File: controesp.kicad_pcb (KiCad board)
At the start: 2 copper layers, 216.9 x 86.5 mm, 71 parts, among them J1 Screw_Terminal_01x08, J13 Conn_01x19_Socket, J14 Conn_01x16_Socket, J15 Screw_Terminal_01x02, J16 Conn_01x19_Socket, J17 Conn_01x19_Socket, J2 Screw_Terminal_01x04, J3 Conn_01x14_Socket, J4 Conn_01x14_Pin, J5 Conn_01x16_Pin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

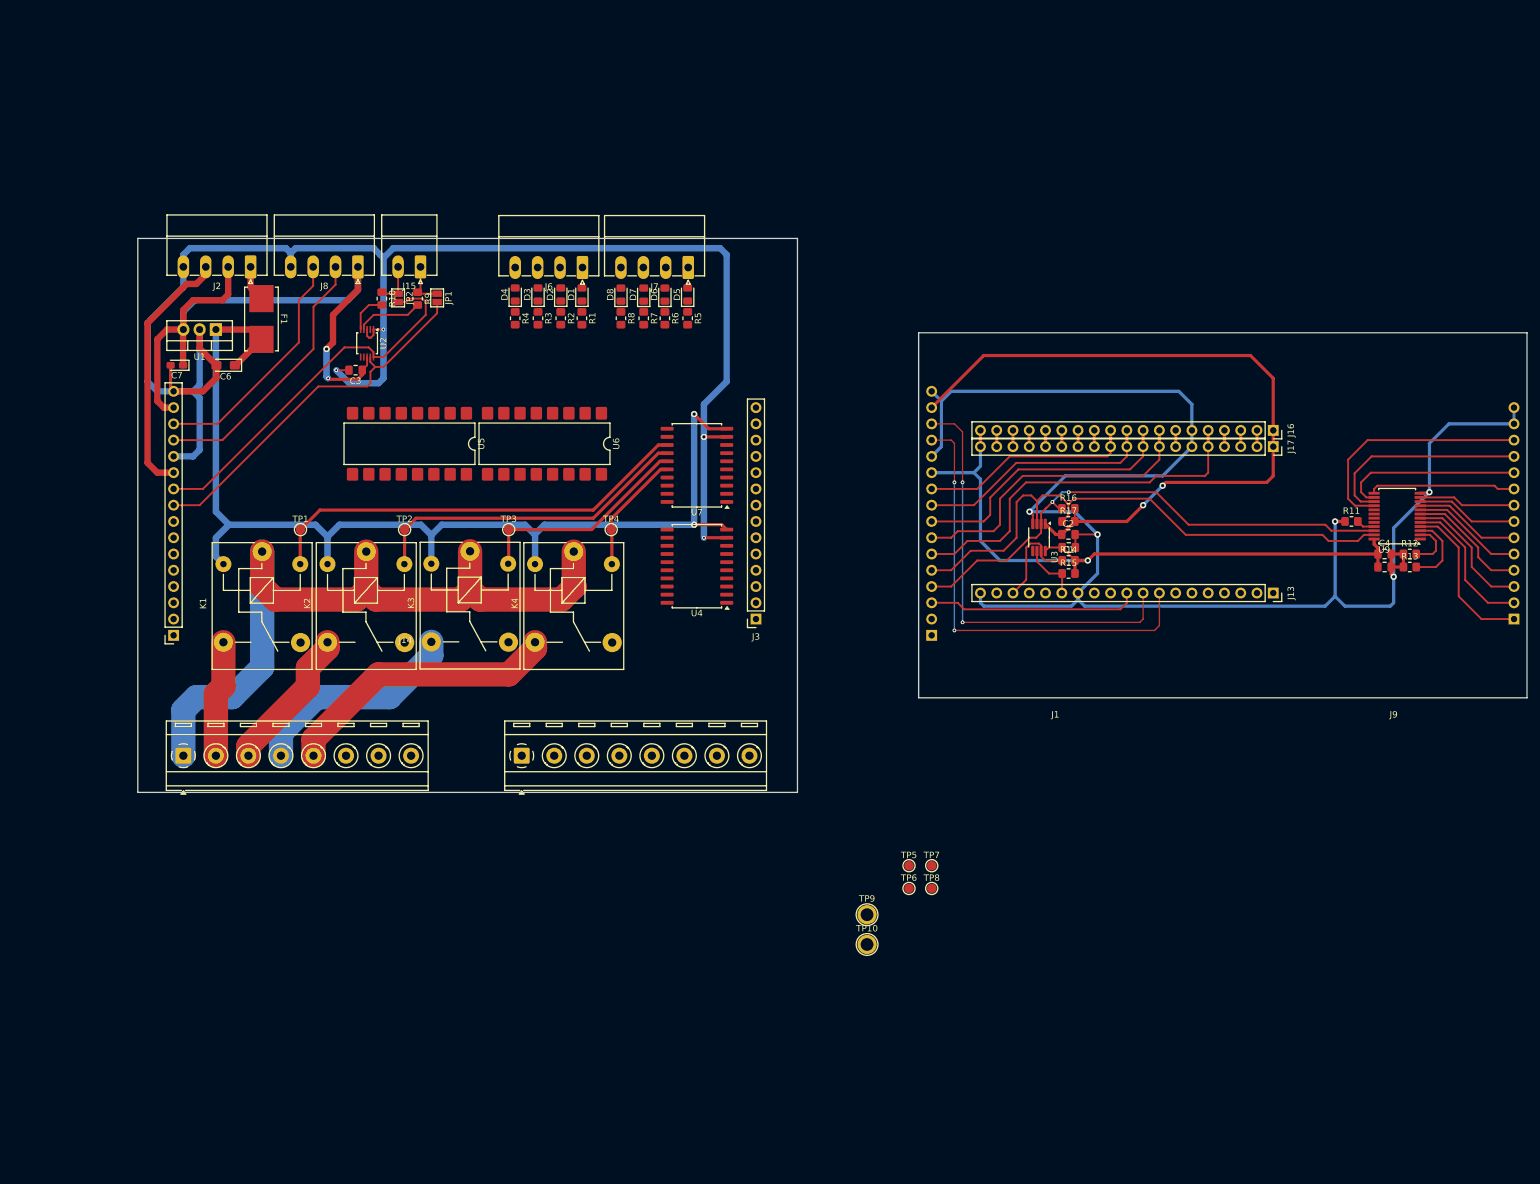
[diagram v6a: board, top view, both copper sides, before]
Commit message: pcb layout finished
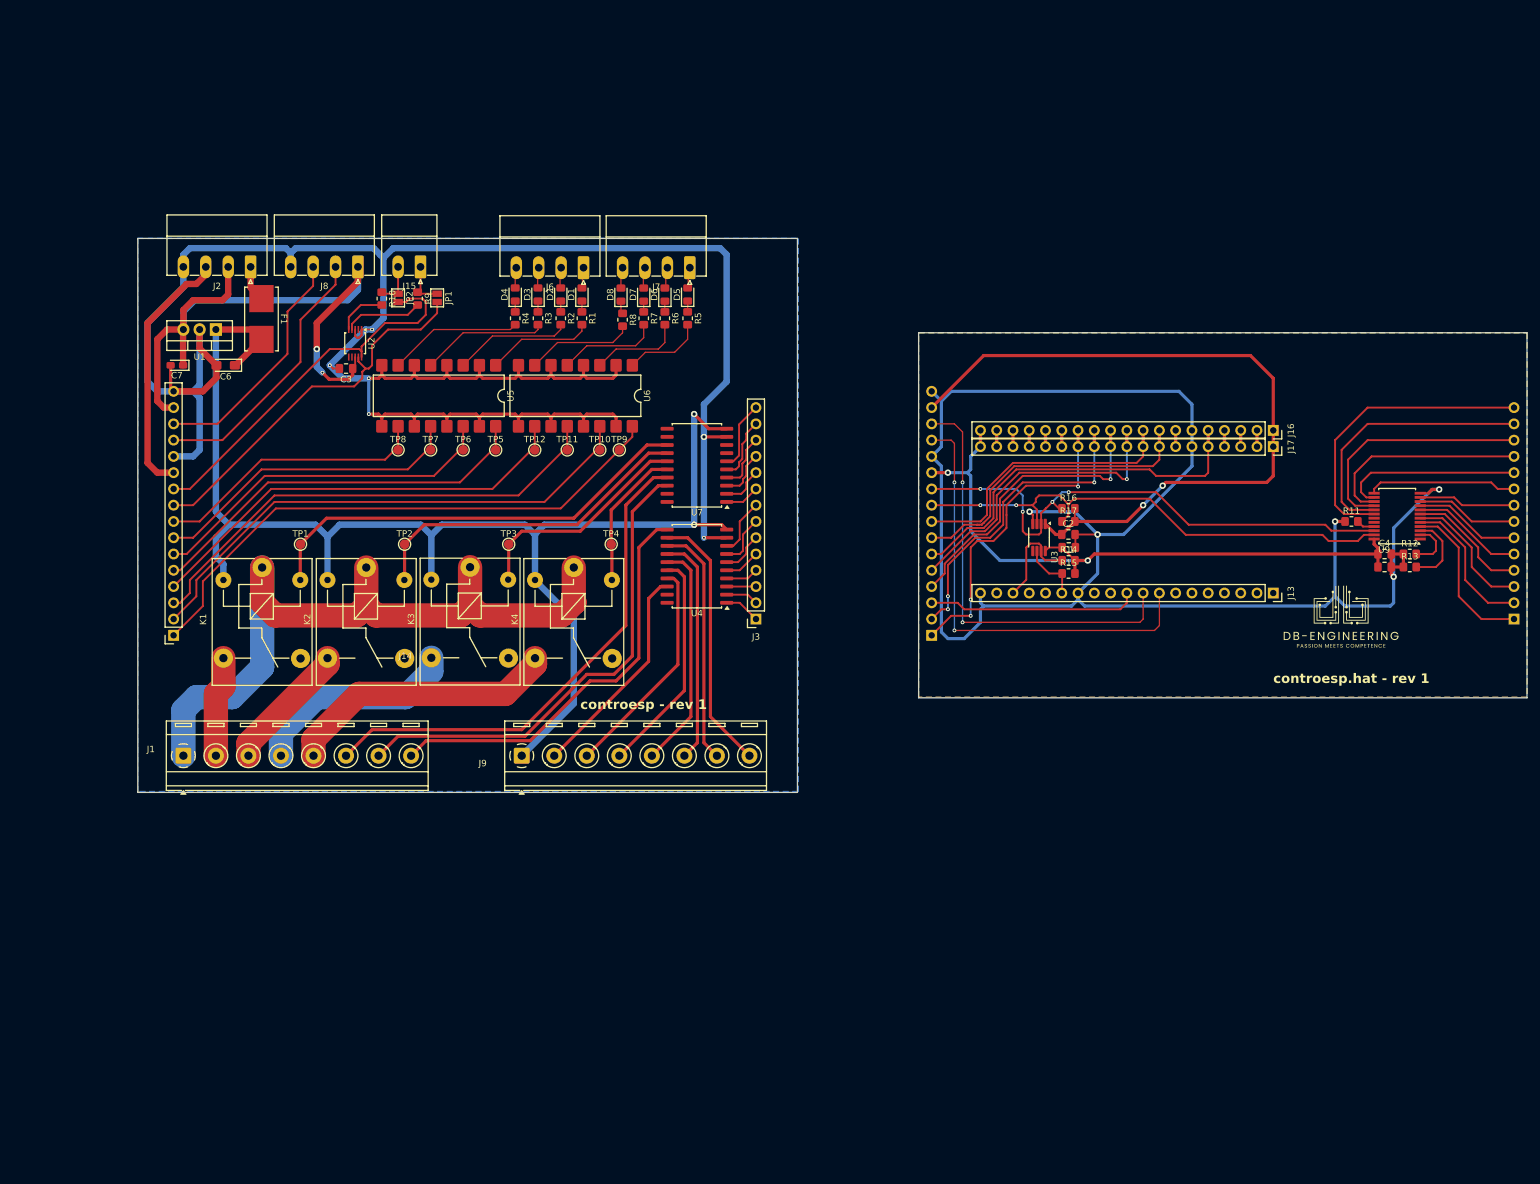
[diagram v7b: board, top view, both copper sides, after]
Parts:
- added G***: LOGO, graphics:db_engineering_logo, F.Cu at (237.7, 109.2)
- added G***: LOGO, graphics:db_engineering_logo, B.Cu at (73.2, 81.3)
- added TP11: ~, TestPoint:TestPoint_Pad_D1.5mm, F.Cu at (116.8, 82.8)
- added TP12: ~, TestPoint:TestPoint_Pad_D1.5mm, F.Cu at (111.8, 82.8)
- TP10: value DO12 -> ~; footprint TestPoint:TestPoint_Plated_Hole_D2.0mm -> TestPoint:TestPoint_Pad_D1.5mm
- TP9: value DO11 -> ~; footprint TestPoint:TestPoint_Plated_Hole_D2.0mm -> TestPoint:TestPoint_Pad_D1.5mm
- moved TP8 107.9 mm to (90.4, 82.8)
- moved TP7 101.7 mm to (95.5, 82.8)
- moved TP6 97.6 mm to (100.6, 82.8)
- moved TP5 91.5 mm to (105.7, 82.8)
- moved TP10 87.8 mm to (121.9, 82.8)
- moved TP9 82.2 mm to (125.0, 82.8)
- moved U6 8.91 mm to (118.1, 74.4)
- moved U5 8.77 mm to (96.8, 74.4)
- moved K1 2.48 mm to (69.2, 101.2)
- moved K2 2.48 mm to (85.5, 101.2)
- moved K3 2.48 mm to (101.7, 101.1)
- moved K4 2.48 mm to (117.9, 101.2)
- moved TP1 2.29 mm to (75.2, 97.5)
- moved TP2 2.29 mm to (91.4, 97.5)
- moved TP3 2.29 mm to (107.7, 97.5)
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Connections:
- J1 pad 6: DO1 -> DO.1
- J1 pad 7: DO2 -> DO.2
- J1 pad 8: DO3 -> DO.3
- J14 pad 1: /input/DI1 -> /input/DI5
- J14 pad 2: /input/DI2 -> /input/DI6
- J14 pad 3: /input/DI8 -> /input/DI7
- J14 pad 4: /input/DI7 -> /input/DI8
- J14 pad 5: /input/DI3 -> /input/DI1
- J14 pad 6: /input/DI4 -> /input/DI2
- J14 pad 7: /input/DI5 -> /input/DI3
- J14 pad 8: /input/DI6 -> /input/DI4
- J3 pad 1: DO1 -> /powerOutput/DO1
- J3 pad 13: unconnected-(J3-Pin_13-Pad13) -> /powerOutput/DO13
- J3 pad 14: unconnected-(J3-Pin_14-Pad14) -> /powerOutput/DO14
- J3 pad 2: DO2 -> /powerOutput/DO2
- J3 pad 3: DO3 -> /powerOutput/DO3
- J3 pad 4: DO4 -> /powerOutput/DO4
- J3 pad 5: DO5 -> /powerOutput/DO5
- J3 pad 6: DO6 -> /powerOutput/DO6
- J3 pad 9: DO9 -> /powerOutput/DO9
- J4 pad 13: /controesp_hat/GND -> /controesp_hat/P14
- J4 pad 14: /controesp_hat/GND -> /controesp_hat/P15
- J5 pad 4: unconnected-(J5-Pin_4-Pad4) -> /controesp_hat/25
- J5 pad 5: unconnected-(J5-Pin_5-Pad5) -> /controesp_hat/26
- J9 pad 1: GND -> +24V
- J9 pad 2: unconnected-(J9-Pin_2-Pad2) -> DO.4
- J9 pad 3: unconnected-(J9-Pin_3-Pad3) -> DO.5
- J9 pad 4: unconnected-(J9-Pin_4-Pad4) -> DO.6
- J9 pad 5: DO9 -> DO.7
- J9 pad 6: DO4 -> DO.8
- J9 pad 7: DO5 -> DO.9
- J9 pad 8: DO6 -> DO.10
- TP10 pad 1: Net-(U7-O4) -> /input/DI6
- TP5 pad 1: Net-(U4-O6) -> /input/DI1
- TP6 pad 1: Net-(U4-O6) -> /input/DI2
- TP7 pad 1: Net-(U4-O7) -> /input/DI3
- TP8 pad 1: Net-(U4-O8) -> /input/DI4
- TP9 pad 1: Net-(U7-O3) -> /input/DI5
- U4 pad 1: DO1 -> /powerOutput/DO1
- U4 pad 11: unconnected-(U4-O8-Pad11) -> DO.3
- U4 pad 12: unconnected-(U4-O7-Pad12) -> DO.10
- U4 pad 13: unconnected-(U4-O6-Pad13) -> DO.9
- U4 pad 14: unconnected-(U4-O5-Pad14) -> DO.8
- U4 pad 15: unconnected-(U4-O4-Pad15) -> DO.7
- U4 pad 16: unconnected-(U4-O3-Pad16) -> DO.6
- U4 pad 17: unconnected-(U4-O2-Pad17) -> DO.5
- U4 pad 18: unconnected-(U4-O1-Pad18) -> DO.4
- U4 pad 2: DO2 -> /powerOutput/DO2
- U4 pad 3: DO3 -> /powerOutput/DO3
- U4 pad 4: DO4 -> /powerOutput/DO4
- U4 pad 5: DO5 -> /powerOutput/DO5
- U4 pad 6: DO6 -> /powerOutput/DO6
- U7 pad 1: DO9 -> /powerOutput/DO9
- U7 pad 17: DO.10 -> DO.1
- U7 pad 18: DO.9 -> DO.2
- U9 pad 17: unconnected-(U9-P14-Pad17) -> /controesp_hat/P14
- U9 pad 18: unconnected-(U9-P15-Pad18) -> /controesp_hat/P15
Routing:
- net GND: track 251.0 -> 363.8 mm, vias 4 -> 6
- net /input/DI5: track 0.00 -> 88.4 mm
- net /input/DI6: track 0.00 -> 82.2 mm
- net DO.1: track 0.00 -> 79.1 mm
- net /input/DI7: track 0.00 -> 75.8 mm
- net DO.2: track 0.00 -> 75.7 mm
- net /input/DI8: track 0.00 -> 68.5 mm
- net DO.3: track 0.00 -> 64.7 mm
- net /input/DI1: track 0.00 -> 61.5 mm
- net /input/DI2: track 0.00 -> 55.3 mm
- net /input/DI3: track 0.00 -> 49.2 mm
- net /controesp_hat/32: track 2.54 -> 49.7 mm, vias 0 -> 3
- net /controesp_hat/P15: track 0.00 -> 46.9 mm
- net /controesp_hat/33: track 2.54 -> 48.5 mm, vias 0 -> 3
- net +24V: track 171.3 -> 214.5 mm
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- added copper zone on B.Cu, net /controesp_hat/GND
- added copper zone on F.Cu, net /controesp_hat/GND
- added copper zone on B.Cu, net GND
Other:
- board text added: "controesp - rev 1"
- board text added: "controesp.hat - rev 1"

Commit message: almost done
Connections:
- J1 pad 2: Net-(J1-Pin_2) -> /powerOutput/230V
- J1 pad 3: Net-(J1-Pin_3) -> /powerOutput/230V
- J1 pad 4: Net-(J1-Pin_4) -> /powerOutput/230V
- J1 pad 5: Net-(J1-Pin_5) -> /powerOutput/230V
- K1 pad 3: Net-(J1-Pin_2) -> /powerOutput/230V
- K2 pad 3: Net-(J1-Pin_3) -> /powerOutput/230V
- K3 pad 3: Net-(J1-Pin_4) -> /powerOutput/230V
- K4 pad 3: Net-(J1-Pin_5) -> /powerOutput/230V
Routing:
- net /powerOutput/230V: track 0.00 -> 112.2 mm
- net Net-(J1-Pin_5): track 42.9 -> 0.00 mm
- net Net-(J1-Pin_4): track 33.1 -> 0.00 mm
- net Net-(J1-Pin_3): track 20.4 -> 0.00 mm
- net Net-(J1-Pin_2): track 15.7 -> 0.00 mm
